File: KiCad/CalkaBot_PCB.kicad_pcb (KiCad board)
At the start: 2 copper layers, 6 parts, among them J1 Conn_01x03_Pin

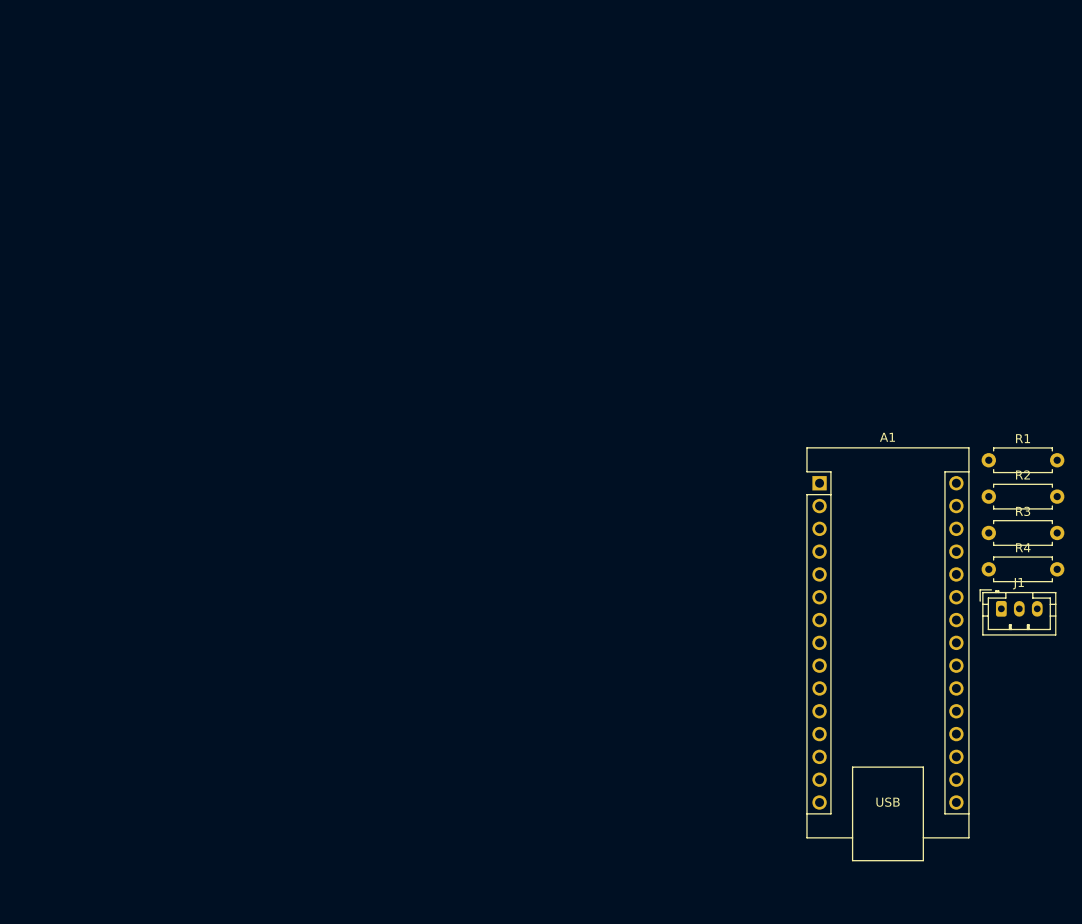
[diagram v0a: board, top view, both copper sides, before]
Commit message: working on screws and holes on pcb
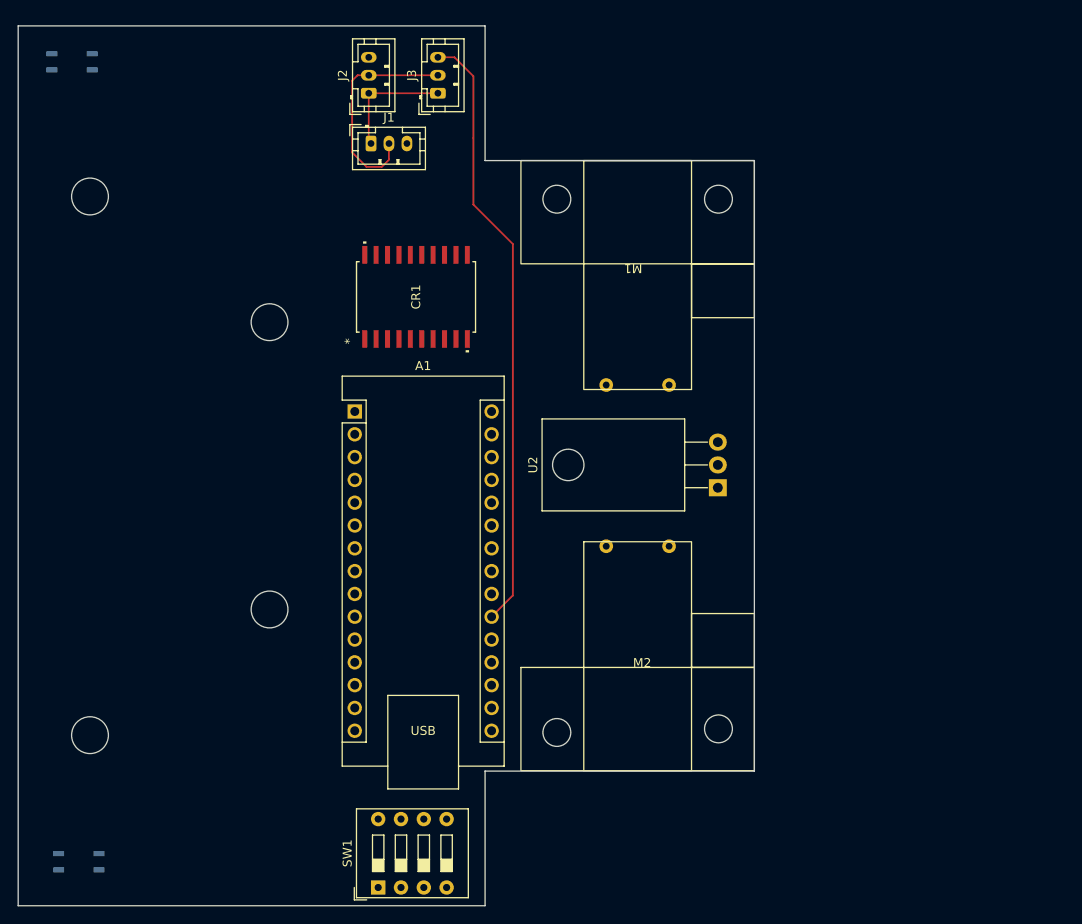
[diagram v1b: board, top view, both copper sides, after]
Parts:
- removed R1, R2, R4: 68R, Resistor_THT:R_Axial_DIN0207_L6.3mm_D2.5mm_P7.62mm_Horizontal
- removed R3: 330R, Resistor_THT:R_Axial_DIN0207_L6.3mm_D2.5mm_P7.62mm_Horizontal
- added CR1: L6225D, L6225D:SO-20_STM, F.Cu at (64.3, 49.2)
- added J2: Conn_01x03_Pin, Connector_JST:JST_PH_B3B-PH-K_1x03_P2.00mm_Vertical, F.Cu at (59.0, 26.5)
- added J3: Conn_01x03_Pin, Connector_JST:JST_PH_B3B-PH-K_1x03_P2.00mm_Vertical, F.Cu at (66.8, 26.5)
- added M1: Motor_Right, CalkaBot3k0:CalkBot3k0_Motor_Right, F.Cu at (102.0, 34.0)
- added M2: Motor_Left, CalkaBot3k0:CalkBot3k0_Motor_Left, F.Cu at (76.0, 102.0)
- added Q1: KTIR0711S, footprints:KTIR0711S_KNB, B.Cu at (26.0, 23.0)
- added Q2: KTIR0711S, footprints:KTIR0711S_KNB, B.Cu at (26.8, 112.1)
- added SW1: SW_DIP_x04, Button_Switch_THT:SW_DIP_SPSTx04_Slide_9.78x12.34mm_W7.62mm_P2.54mm, F.Cu at (60.1, 115.0)
- added U2: L7805, Package_TO_SOT_THT:TO-220-3_Horizontal_TabDown, F.Cu at (97.9, 70.4)
- A1: value Arduino_Nano_v3.x -> Arduino_Nano_v2.x
- moved J1 87.3 mm to (59.3, 32.1)
- moved A1 52.4 mm to (57.5, 62.0)
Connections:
- A1 pad 19: unconnected-(A1-A0-Pad19) -> Net-(A1-A0)
- A1 pad 20: unconnected-(A1-A1-Pad20) -> Net-(A1-A1)
- A1 pad 21: unconnected-(A1-A2-Pad21) -> Net-(A1-A2)
- A1 pad 30: unconnected-(A1-VIN-Pad30) -> Net-(A1-VIN)
- A1 pad 4: unconnected-(A1-GND-Pad4) -> Net-(J1-Pin_2)
- J1 pad 1: unconnected-(J1-Pin_1-Pad1) -> Net-(A1-VIN)
- J1 pad 2: unconnected-(J1-Pin_2-Pad2) -> Net-(J1-Pin_2)
- J1 pad 3: unconnected-(J1-Pin_3-Pad3) -> Net-(A1-A0)
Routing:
- net Net-(A1-A2): track 0.00 -> 67.8 mm
- net Net-(J1-Pin_2): track 0.00 -> 24.7 mm
- net Net-(A1-VIN): track 0.00 -> 13.4 mm
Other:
- board outline added: 82 x 98 mm

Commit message: working on PCB + changes within NX for project review
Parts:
- removed U2: L7805, Package_TO_SOT_THT:TO-220-3_Horizontal_TabDown
- added R1: 20k, Resistor_SMD:R_0805_2012Metric_Pad1.20x1.40mm_HandSolder, F.Cu at (33.5, 20.8)
- added R3: 20k, Resistor_SMD:R_0805_2012Metric_Pad1.20x1.40mm_HandSolder, F.Cu at (33.8, 108.2)
- added R4: 220, Resistor_SMD:R_0805_2012Metric_Pad1.20x1.40mm_HandSolder, F.Cu at (33.4, 26.7)
- added R5: 220, Resistor_SMD:R_0805_2012Metric_Pad1.20x1.40mm_HandSolder, F.Cu at (34.0, 114.1)
- added U1: L78M05CDT-TR, L78M05CDT-TR:VREG_L78M05CDT-TR, F.Cu at (86.4, 70.6)
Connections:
- net Net-(A1-VIN) renamed +5V
- A1 pad 22: unconnected-(A1-A3-Pad22) -> Net-(A1-A3)
- A1 pad 23: unconnected-(A1-A4-Pad23) -> Net-(A1-A4)
- A1 pad 4: Net-(J1-Pin_2) -> GND
- J1 pad 2: Net-(J1-Pin_2) -> GND
- J2 pad 2: Net-(J1-Pin_2) -> GND
- J3 pad 2: Net-(J1-Pin_2) -> GND
- Q1 pad 1: unconnected-(Q1-Pad1) -> Net-(Q1-Pad1)
- Q1 pad 2: unconnected-(Q1-Pad2) -> Net-(A1-A4)
- Q1 pad 3: unconnected-(Q1-Pad3) -> GND
- Q1 pad 4: unconnected-(Q1-Pad4) -> GND
- Q2 pad 1: unconnected-(Q2-Pad1) -> Net-(Q2-Pad1)
- Q2 pad 2: unconnected-(Q2-Pad2) -> Net-(A1-A3)
- Q2 pad 3: unconnected-(Q2-Pad3) -> GND
- Q2 pad 4: unconnected-(Q2-Pad4) -> GND
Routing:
- net Net-(J1-Pin_2): track 24.7 -> 0.00 mm
- net GND: track 0.00 -> 24.7 mm

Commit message: w trakcie ukladania elementow
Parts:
- added C1: 0u33, Capacitor_SMD:C_0805_2012Metric_Pad1.18x1.45mm_HandSolder, B.Cu at (55.3, 41.1)
- added C11: 0u1, Capacitor_SMD:C_0805_2012Metric_Pad1.18x1.45mm_HandSolder, F.Cu at (114.5, 47.6)
- added C12: 0u1, Capacitor_SMD:C_0805_2012Metric_Pad1.18x1.45mm_HandSolder, F.Cu at (114.5, 50.6)
- added C2: 0u1, Capacitor_SMD:C_0805_2012Metric_Pad1.18x1.45mm_HandSolder, B.Cu at (55.3, 46.1)
- added C3: 10n, Capacitor_SMD:C_0805_2012Metric_Pad1.18x1.45mm_HandSolder, F.Cu at (113.6, 59.9)
- added C4: 200n, Capacitor_SMD:C_0805_2012Metric_Pad1.18x1.45mm_HandSolder, F.Cu at (113.4, 64.6)
- added C5: 5n6, Capacitor_SMD:C_0805_2012Metric_Pad1.18x1.45mm_HandSolder, F.Cu at (113.4, 67.6)
- added C6: 5n6, Capacitor_SMD:C_0805_2012Metric_Pad1.18x1.45mm_HandSolder, F.Cu at (113.4, 70.6)
- added C7: 0u1, Capacitor_SMD:C_0805_2012Metric_Pad1.18x1.45mm_HandSolder, F.Cu at (113.4, 73.6)
- added C8: 100u, Capacitor_SMD:CP_Elec_8x10.5, F.Cu at (77.6, 52.1)
- added C9: 0u1, Capacitor_SMD:C_0805_2012Metric_Pad1.18x1.45mm_HandSolder, B.Cu at (54.1, 58.1)
- added D1: 1N4148WT, Diode_SMD:D_SOD-523, F.Cu at (117.6, 64.1)
- added D2: 1N4148WT, Diode_SMD:D_SOD-523, F.Cu at (117.6, 66.6)
- added D3: SS14, Diode_SMD:D_SMA_Handsoldering, B.Cu at (53.1, 33.3)
- added J4: Conn_01x02_Pin, Connector_PinHeader_2.54mm:PinHeader_1x02_P2.54mm_Vertical, F.Cu at (60.1, 36.3)
- added J5: MOTOR3, Connector_PinHeader_2.54mm:PinHeader_1x02_P2.54mm_Vertical, F.Cu at (70.1, 37.8)
- added J6: StartModule, Connector_PinHeader_2.54mm:PinHeader_1x03_P2.54mm_Vertical, F.Cu at (69.2, 49.9)
- added Q3: IRLL014NTRPBF, Package_TO_SOT_SMD:SOT-223, F.Cu at (61.0, 53.0)
- added R2: 100R, Resistor_SMD:R_0805_2012Metric_Pad1.20x1.40mm_HandSolder, F.Cu at (118.2, 55.5)
- added R6: 100k, Resistor_SMD:R_0805_2012Metric_Pad1.20x1.40mm_HandSolder, F.Cu at (118.2, 58.5)
- added R7: 100k, Resistor_SMD:R_0805_2012Metric_Pad1.20x1.40mm_HandSolder, F.Cu at (118.2, 61.4)
- CR1: value L6225D -> L6225PD; footprint L6225D:SO-20_STM -> Package_SO:SO-20-1EP_7.52x12.825mm_P1.27mm_EP6.045x12.09mm_Mask3.56x4.47mm_ThermalVias
- R1, R3, R4, R5: moved to B.Cu
- moved U1 35.1 mm to (63.9, 43.7)
- moved CR1 32.1 mm to (89.8, 68.7), turned to -90 degrees
- moved J1 10.1 mm to (69.4, 32.8), turned to 180 degrees
- moved J2 4.48 mm to (60.9, 22.4), turned to -90 degrees
- moved J3 4.27 mm to (68.0, 22.4), turned to -90 degrees
- moved R3 2.83 mm to (31.9, 110.3)
- moved R5 2.12 mm to (31.9, 113.8)
- moved R1 1.41 mm to (33.3, 22.2)
- moved Q2 1.37 mm to (25.4, 112.3)
- moved Q1 0.85 mm to (26.6, 23.6)
- moved R4 0.61 mm to (33.3, 27.3)
- moved SW1 0.50 mm to (60.1, 115.5)
- moved A1 0.49 mm to (57.3, 62.4)
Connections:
- net Net-(A1-A3) renamed FLOOR_SENSOR_RIGHT
- net Net-(A1-A4) renamed FLOOR_SENSOR_LEFT
- A1 pad 10: unconnected-(A1-D7-Pad10) -> M_FRONT
- A1 pad 11: unconnected-(A1-D8-Pad11) -> M_ENB
- A1 pad 12: unconnected-(A1-D9-Pad12) -> M_ENA
- A1 pad 13: unconnected-(A1-D10-Pad13) -> M_IN2B
- A1 pad 14: unconnected-(A1-D11-Pad14) -> M_IN1B
- A1 pad 15: unconnected-(A1-D12-Pad15) -> M_IN2A
- A1 pad 16: unconnected-(A1-D13-Pad16) -> M_IN1A
- A1 pad 29: unconnected-(A1-GND-Pad29) -> GND
- A1 pad 9: unconnected-(A1-D6-Pad9) -> START_MODULE
- CR1 pad 1: unconnected-(CR1-IN1A-Pad1) -> GND
- CR1 pad 10: unconnected-(CR1-IN2B-Pad10) -> GND
- CR1 pad 11: unconnected-(CR1-ENB-Pad11) -> GND
- CR1 pad 12: unconnected-(CR1-VBOOT-Pad12) -> Net-(CR1-OUT1B)
- CR1 pad 13: unconnected-(CR1-OUT2B-Pad13) -> GND
- CR1 pad 14: unconnected-(CR1-VSB-Pad14) -> M_IN1B
- CR1 pad 15: unconnected-(CR1-GND-Pad15) -> M_IN2B
- CR1 pad 16: unconnected-(CR1-GND-Pad16) -> Net-(CR1-ENB)
- CR1 pad 17: unconnected-(CR1-VSA-Pad17) -> Net-(CR1-VBOOT)
- CR1 pad 18: unconnected-(CR1-OUT2A-Pad18) -> Net-(CR1-OUT2B)
- CR1 pad 19: unconnected-(CR1-VCP-Pad19) -> MotorPower
- CR1 pad 2: unconnected-(CR1-IN2A-Pad2) -> MotorPower
- CR1 pad 20: unconnected-(CR1-ENA-Pad20) -> GND
- CR1 pad 3: unconnected-(CR1-SENSEA-Pad3) -> Net-(CR1-OUT2A)
- CR1 pad 4: unconnected-(CR1-OUT1A-Pad4) -> Net-(CR1-VCP)
- CR1 pad 5: unconnected-(CR1-GND-Pad5) -> Net-(CR1-ENA)
- CR1 pad 6: unconnected-(CR1-GND-Pad6) -> M_IN1A
- CR1 pad 7: unconnected-(CR1-OUT1B-Pad7) -> M_IN2A
- CR1 pad 8: unconnected-(CR1-SENSEB-Pad8) -> GND
- CR1 pad 9: unconnected-(CR1-IN1B-Pad9) -> Net-(CR1-OUT1A)
- M1 pad 1: unconnected-(M1-+-Pad1) -> Net-(CR1-OUT2A)
- M1 pad 2: unconnected-(M1---Pad2) -> Net-(CR1-OUT1A)
- M2 pad 1: unconnected-(M2-+-Pad1) -> Net-(CR1-OUT1B)
- M2 pad 2: unconnected-(M2---Pad2) -> Net-(CR1-OUT2B)
- SW1 pad 1: unconnected-(SW1-Pad1) -> GND
- SW1 pad 2: unconnected-(SW1-Pad2) -> GND
- SW1 pad 3: unconnected-(SW1-Pad3) -> GND
- SW1 pad 4: unconnected-(SW1-Pad4) -> GND
- U1 pad 1: +7.5V -> MotorPower
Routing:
- net Net-(A1-A2): track 67.8 -> 0.00 mm
- net GND: track 24.7 -> 0.00 mm
- net +5V: track 13.4 -> 0.00 mm

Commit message: PCB finished ready to send
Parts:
- C1, C2, C9: moved to F.Cu
- C11, C12: moved to B.Cu
- moved R7 45.2 mm to (78.8, 83.6), turned to -90 degrees
- moved R6 43.6 mm to (78.0, 75.5), turned to 180 degrees
- moved C12 38.1 mm to (89.1, 79.0), turned to 180 degrees
- moved C6 33.8 mm to (80.9, 80.0), turned to -90 degrees
- moved C5 33.6 mm to (80.9, 76.1), turned to 90 degrees
- moved R2 29.7 mm to (99.3, 78.5), turned to -90 degrees
- moved C11 27.0 mm to (89.2, 57.2)
- moved C3 26.5 mm to (99.3, 82.3), turned to -90 degrees
- moved D2 25.6 mm to (96.7, 81.3), turned to 90 degrees
- moved D1 21.0 mm to (99.6, 75.0), turned to 90 degrees
- moved D3 20.9 mm to (72.5, 41.2)
- moved C7 20.9 mm to (98.3, 59.2)
- moved C4 20.6 mm to (96.6, 76.5), turned to -90 degrees
- moved C9 13.3 mm to (64.9, 50.3), turned to 90 degrees
- moved C8 12.9 mm to (80.1, 64.8), turned to 90 degrees
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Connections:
- A1 pad 10: M_FRONT -> Net-(A1-D7)
- A1 pad 11: M_ENB -> M_IN2A
- A1 pad 12: M_ENA -> M_IN1A
- A1 pad 13: M_IN2B -> M_IN1B
- A1 pad 14: M_IN1B -> M_IN2B
- A1 pad 15: M_IN2A -> M_ENB
- A1 pad 16: M_IN1A -> M_ENA
- A1 pad 19: Net-(A1-A0) -> FLOOR_SENSOR_RIGHT
- A1 pad 20: Net-(A1-A1) -> FLOOR_SENSOR_LEFT
- A1 pad 22: FLOOR_SENSOR_RIGHT -> Net-(A1-A3)
- A1 pad 23: FLOOR_SENSOR_LEFT -> Net-(A1-A4)
- A1 pad 5: unconnected-(A1-D2-Pad5) -> START_MODULE
- A1 pad 6: unconnected-(A1-D3-Pad6) -> M_FRONT
- A1 pad 7: unconnected-(A1-D4-Pad7) -> Net-(A1-D4)
- A1 pad 8: unconnected-(A1-D5-Pad8) -> Net-(A1-D5)
- A1 pad 9: START_MODULE -> Net-(A1-D6)
- CR1 pad 21: (no net) -> GND
- J1 pad 3: Net-(A1-A0) -> Net-(A1-A4)
- J2 pad 3: Net-(A1-A1) -> Net-(A1-A2)
- J3 pad 3: Net-(A1-A2) -> Net-(A1-A3)
- SW1 pad 5: unconnected-(SW1-Pad5) -> Net-(A1-D7)
- SW1 pad 6: unconnected-(SW1-Pad6) -> Net-(A1-D6)
- SW1 pad 7: unconnected-(SW1-Pad7) -> Net-(A1-D5)
- SW1 pad 8: unconnected-(SW1-Pad8) -> Net-(A1-D4)
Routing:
- net GND: track 0.00 -> 409.4 mm, vias 0 -> 1
- net +5V: track 0.00 -> 225.9 mm, vias 0 -> 1
- net Net-(A1-A3): track 0.00 -> 138.7 mm, vias 0 -> 1
- net Net-(A1-A2): track 0.00 -> 134.0 mm, vias 0 -> 1
- net Net-(A1-A4): track 0.00 -> 132.5 mm, vias 0 -> 1
- net FLOOR_SENSOR_LEFT: track 0.00 -> 132.4 mm, vias 0 -> 1
- net MotorPower: track 0.00 -> 114.7 mm, vias 0 -> 3
- net M_IN2A: track 0.00 -> 74.7 mm, vias 0 -> 1
- net M_IN1A: track 0.00 -> 73.5 mm, vias 0 -> 1
- net M_IN1B: track 0.00 -> 65.0 mm, vias 0 -> 1
- net M_IN2B: track 0.00 -> 64.0 mm, vias 0 -> 1
- net FLOOR_SENSOR_RIGHT: track 0.00 -> 58.3 mm, vias 0 -> 1
- net M_ENB: track 0.00 -> 38.1 mm, vias 0 -> 1
- net Net-(A1-D4): track 0.00 -> 36.7 mm
- net Net-(A1-D5): track 0.00 -> 35.8 mm
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- added copper zone on B.Cu, net GND

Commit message: płytka leci a rece sa gotowe do druku
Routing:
- added copper zone on F.Cu, net GND
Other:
- board text added: "CalkaBot 3k0 by JakubKivi"
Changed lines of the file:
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@@
 			(outputformat 1)
 			(mirror no)
-			(drillshape 1)
+			(drillshape 0)
 			(scaleselection 1)
-			(outputdirectory "")
+			(outputdirectory "Export/")
 		)
 	)
@@
 		(tags "Diode SOD523")
 		(property "Reference" "D1"
-			(at 0 -1.3 -90)
+			(at 0.2 1.5 -90)
 			(layer "F.SilkS")
 			(effects
@@
 		(tags "capacitor handsolder")
 		(property "Reference" "C4"
-			(at 0 -1.68 90)
+			(at 0.1 1.8 90)
 			(layer "F.SilkS")
 			(effects
@@
 		)
 	)
-	(gr_rect
-		(start 20 19)
-		(end 55.5 117)
-		(stroke
-			(width 0.3)
-			(type solid)
-		)
-		(fill none)
-		(layer "F.Adhes")
-	)
 	(gr_circle
 		(center 80 38.3)
@@
 		(layer "Edge.Cuts")
 	)
+	(gr_text "CalkaBot 3k0\nby JakubKivi"
+		(at 25.8 68.1 270)
+		(layer "B.Cu" knockout)
+		(effects
+			(font
+				(size 3 3)
+				(thickness 0.6)
+				(bold yes)
+			)
+			(justify bottom mirror)
+		)
+	)
 	(segment
 		(start 81.1375 79.2)
@@
 		(net 1)
 		(net_name "GND")
-		(layer "B.Cu")
+		(layer "F.Cu")
 		(hatch edge 0.5)
+		(priority 2)
 		(connect_pads
 			(clearance 0.5)
@@
 		(polygon
 			(pts
+				(xy 20 19) (xy 72 19) (xy 72 34) (xy 102 34) (xy 102 102) (xy 72 102) (xy 72 117) (xy 20 117)
+			)
+		)
+	)
+	(zone
+		(net 1)
+		(net_name "GND")
+		(layer "B.Cu")
+		(hatch edge 0.5)
+		(connect_pads
+			(clearance 0.5)
+		)
+		(min_thickness 0.25)
+		(filled_areas_thickness no)
+		(fill yes
+			(thermal_gap 0.5)
+			(thermal_bridge_width 0.5)
+		)
+		(polygon
+			(pts
 				(xy 97.4 65) (xy 97.4 72) (xy 96.4 72.9) (xy 81.8 72.9) (xy 91.7 62.9) (xy 95.3 62.9)
 			)
 		)
+	)
+	(zone
+		(net 1)
+		(net_name "GND")
+		(layer "B.Cu")
+		(hatch edge 0.5)
+		(priority 1)
+		(connect_pads
+			(clearance 0.5)
+		)
+		(min_thickness 0.25)
+		(filled_areas_thickness no)
+		(fill yes
+			(thermal_gap 0.5)
+			(thermal_bridge_width 0.5)
+			(island_removal_mode 1)
+			(island_area_min 10)
+		)
+		(polygon
+			(pts
+				(xy 20 19) (xy 72 19) (xy 72 34) (xy 102 34) (xy 102 102) (xy 72 102) (xy 72 117) (xy 20 117)
+			)
+		)

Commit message: wyslano druga plytke pisze sie praca i program
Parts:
- added D4: LED, LED_SMD:LED_0805_2012Metric_Pad1.15x1.40mm_HandSolder, F.Cu at (80.6, 81.0)
- added R8: 10k, Resistor_SMD:R_0805_2012Metric_Pad1.20x1.40mm_HandSolder, F.Cu at (73.7, 55.2)
- added R9: 10k, Resistor_SMD:R_0805_2012Metric_Pad1.20x1.40mm_HandSolder, F.Cu at (77.4, 82.0)
- C5, C6, R6, R7: moved to B.Cu
- C8: footprint Capacitor_SMD:CP_Elec_8x10.5 -> Capacitor_SMD:CP_Elec_6.3x7.7
- CR1: footprint Package_SO:SO-20-1EP_7.52x12.825mm_P1.27mm_EP6.045x12.09mm_Mask3.56x4.47mm_ThermalVias -> CalkaBot3k0:L6225PD
- Q1, Q2: footprint footprints:KTIR0711S_KNB -> CalkaBot3k0:KTIR0711S
- Q3: value IRLL014NTRPBF -> BS108; footprint Package_TO_SOT_SMD:SOT-223 -> CalkaBot3k0:SOT-223-IRLL014NTRPBF
- moved R5 93.5 mm to (31.8, 20.3)
- moved Q1 90.4 mm to (24.0, 114.0)
- moved Q2 90.3 mm to (24.0, 22.0)
- moved R1 90.0 mm to (30.0, 113.8), turned to 180 degrees
- moved R3 85.5 mm to (31.8, 24.9), turned to 180 degrees
- moved R4 82.2 mm to (22.0, 108.7), turned to 90 degrees
- moved C5 18.8 mm to (76.7, 57.8), turned to 0 degrees
- moved R6 15.5 mm to (76.7, 60.1)
- moved C8 7.20 mm to (78.4, 57.8)
- moved C6 5.74 mm to (80.2, 85.7)
- moved R7 5.61 mm to (79.1, 89.2), turned to 180 degrees
- moved D1 5.36 mm to (98.5, 80.2)
- moved C3 4.54 mm to (100.7, 78.0), turned to 90 degrees
- moved Q3 4.46 mm to (77.8, 49.3), turned to 180 degrees
- moved C4 3.86 mm to (96.4, 80.3)
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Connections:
- A1 pad 19: FLOOR_SENSOR_RIGHT -> FLOOR_SENSOR_LEFT
- A1 pad 20: FLOOR_SENSOR_LEFT -> FLOOR_SENSOR_RIGHT
- A1 pad 24: unconnected-(A1-A5-Pad24) -> Net-(A1-A5)
- A1 pad 27: unconnected-(A1-+5V-Pad27) -> +5V
- A1 pad 30: +5V -> unconnected-(A1-VIN-Pad30)
- D3 pad 1: Net-(D3-K) -> MotorPower
- D3 pad 2: GND -> Net-(D3-A)
- J5 pad 1: GND -> MotorPower
- J5 pad 2: Net-(D3-K) -> Net-(D3-A)
- Q1 pad 2: FLOOR_SENSOR_LEFT -> GND
- Q1 pad 3: GND -> FLOOR_SENSOR_LEFT
- Q2 pad 2: FLOOR_SENSOR_RIGHT -> GND
- Q2 pad 3: GND -> FLOOR_SENSOR_RIGHT
- Q3 pad 1: Net-(D3-K) -> Net-(D3-A)
- Q3 pad 3: MotorPower -> GND
- R1 pad 1: FLOOR_SENSOR_LEFT -> +5V
- R1 pad 2: +5V -> FLOOR_SENSOR_LEFT
- R3 pad 1: FLOOR_SENSOR_RIGHT -> +5V
- R3 pad 2: +5V -> FLOOR_SENSOR_RIGHT
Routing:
- net FLOOR_SENSOR_RIGHT: track 58.3 -> 133.9 mm
- net FLOOR_SENSOR_LEFT: track 132.4 -> 63.9 mm
- net MotorPower: track 114.7 -> 154.4 mm
- net Net-(D3-A): track 0.00 -> 27.7 mm
- net GND: track 409.4 -> 431.6 mm
- net Net-(D3-K): track 15.1 -> 0.00 mm, vias 1 -> 0
- net M_ENA: track 24.3 -> 38.7 mm
- net Net-(CR1-ENA): track 29.6 -> 17.1 mm, vias 2 -> 1
- net Net-(CR1-ENB): track 20.3 -> 29.0 mm, vias 0 -> 1
- net Net-(A1-A5): track 0.00 -> 6.89 mm
- net Net-(Q2-Pad1): track 3.50 -> 9.78 mm
- net M_ENB: track 38.1 -> 31.9 mm, vias 1 -> 0
- net M_FRONT: track 33.4 -> 39.5 mm
- net M_IN1A: track 73.5 -> 77.8 mm
- net M_IN1B: track 65.0 -> 61.0 mm
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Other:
- outline, holes or cut-outs redrawn
